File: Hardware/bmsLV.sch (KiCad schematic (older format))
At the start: 34 parts, among them J1 Conn_01x06_Male, J13 Conn_01x04_Male, J2 USB_B_Mini, J3 Conn_01x02_Female, J5 Conn_01x02_Female, K1 RM85V7, Q1 BSS138, SW1 SW_Push, U1 STM32F103C8Tx, Y1 Crystal

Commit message: Dash Led and jumpers
-output to Dash Led created
-added another jumper (J17) to ground
-J14, J15, J16 jumper position changed
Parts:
- added Q8: BSS138, Package_TO_SOT_SMD:SOT-23, symbol Transistor_FET:BSS138
- added R10: 100, Resistor_SMD:R_1206_3216Metric, symbol Device:R_Small
- added R17: 100K, Resistor_SMD:R_1206_3216Metric, symbol Device:R_Small
- added R41: 30, Resistor_SMD:R_1206_3216Metric, symbol Device:R_Small
- R39, R40: value 27 -> 30
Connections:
- net labels added: LED_D, LED_D_OUT
- wire segments 99 -> 106
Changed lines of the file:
@@
 EESchema Schematic File Version 4
-LIBS:bmsLV-cache
 EELAYER 30 0
 EELAYER END
@@
 $EndComp
 $Comp
-L Device:LED D4
-U 1 1 5FFAB034
-P 3750 5150
-F 0 "D4" H 3743 5366 50  0000 C CNN
-F 1 "LED" H 3743 5275 50  0000 C CNN
-F 2 "LED_SMD:LED_1206_3216Metric" H 3750 5150 50  0001 C CNN
-F 3 "~" H 3750 5150 50  0001 C CNN
-	1    3750 5150
-	-1   0    0    1
-$EndComp
-$Comp
 L Device:R_Small R4
 U 1 1 5FFAB03A
@@
 	-1   0    0    1
 $EndComp
-$Comp
-L power:GND #PWR?
-U 1 1 5FFFFAC8
-P 8300 2400
-AR Path="/5FAD7AC5/5FFFFAC8" Ref="#PWR?"  Part="1"
-AR Path="/5FFFFAC8" Ref="#PWR0101"  Part="1"
-F 0 "#PWR0101" H 8300 2150 50  0001 C CNN
-F 1 "GND" H 8305 2227 50  0000 C CNN
-F 2 "" H 8300 2400 50  0001 C CNN
-F 3 "" H 8300 2400 50  0001 C CNN
-	1    8300 2400
-	1    0    0    -1
-$EndComp
-Wire Wire Line
-	8300 2400 8150 2400
 Wire Wire Line
 	8150 2300 8300 2300
@@
 P 5800 5150
 F 0 "R39" V 5604 5150 50  0000 C CNN
-F 1 "27" V 5695 5150 50  0000 C CNN
+F 1 "30" V 5695 5150 50  0000 C CNN
 F 2 "Resistor_SMD:R_1206_3216Metric" H 5800 5150 50  0001 C CNN
 F 3 "~" H 5800 5150 50  0001 C CNN
@@
 P 5800 5250
 F 0 "R40" V 5604 5250 50  0000 C CNN
-F 1 "27" V 5695 5250 50  0000 C CNN
+F 1 "30" V 5695 5250 50  0000 C CNN
 F 2 "Resistor_SMD:R_1206_3216Metric" H 5800 5250 50  0001 C CNN
 F 3 "~" H 5800 5250 50  0001 C CNN
@@
 Wire Wire Line
 	5900 5250 6100 5250
+$Comp
+L Device:R_Small R17
+U 1 1 6076C183
+P 10250 4050
+F 0 "R17" H 10191 4004 50  0000 R CNN
+F 1 "100K" H 10191 4095 50  0000 R CNN
+F 2 "Resistor_SMD:R_1206_3216Metric" H 10250 4050 50  0001 C CNN
+F 3 "~" H 10250 4050 50  0001 C CNN
+	1    10250 4050
+	-1   0    0    1
+$EndComp
+Wire Wire Line
+	10250 4150 10250 4300
+$Comp
+L Device:R_Small R10
+U 1 1 60783A76
+P 10000 3800
+F 0 "R10" V 9804 3800 50  0000 C CNN
+F 1 "100" V 9895 3800 50  0000 C CNN
+F 2 "Resistor_SMD:R_1206_3216Metric" H 10000 3800 50  0001 C CNN
+F 3 "~" H 10000 3800 50  0001 C CNN
+	1    10000 3800
+	0    1    1    0
+$EndComp
+$Comp
+L Transistor_FET:BSS138 Q8
+U 1 1 60791F4D
+P 10650 3800
+F 0 "Q8" H 10855 3754 50  0000 L CNN
+F 1 "BSS138" H 10855 3845 50  0000 L CNN
+F 2 "Package_TO_SOT_SMD:SOT-23" H 10850 3725 50  0001 L CIN
+F 3 "https://www.fairchildsemi.com/datasheets/BS/BSS138.pdf" H 10650 3800 50  0001 L CNN
+	1    10650 3800
+	1    0    0    -1
+$EndComp
+$Comp
+L power:GND #PWR0108
+U 1 1 607B5692
+P 10750 4050
+F 0 "#PWR0108" H 10750 3800 50  0001 C CNN
+F 1 "GND" H 10755 3877 50  0000 C CNN
+F 2 "" H 10750 4050 50  0001 C CNN
+F 3 "" H 10750 4050 50  0001 C CNN
+	1    10750 4050
+	1    0    0    -1
+$EndComp
+$Comp
+L power:GND #PWR0101
+U 1 1 607DED82
+P 10250 4300
+F 0 "#PWR0101" H 10250 4050 50  0001 C CNN
+F 1 "GND" H 10255 4127 50  0000 C CNN
+F 2 "" H 10250 4300 50  0001 C CNN
+F 3 "" H 10250 4300 50  0001 C CNN
+	1    10250 4300
+	1    0    0    -1
+$EndComp
+Wire Wire Line
+	10750 4050 10750 4000
+Wire Wire Line
+	10450 3800 10250 3800
+Wire Wire Line
+	10250 3800 10250 3950
+Wire Wire Line
+	10250 3800 10100 3800
+Connection ~ 10250 3800
+Wire Wire Line
+	9900 3800 9800 3800
+$Comp
+L Device:LED D4
+U 1 1 5FFAB034
+P 3750 5150
+F 0 "D4" H 3743 5366 50  0000 C CNN
+F 1 "LED" H 3743 5275 50  0000 C CNN
+F 2 "LED_SMD:LED_1206_3216Metric" H 3750 5150 50  0001 C CNN
+F 3 "~" H 3750 5150 50  0001 C CNN
+	1    3750 5150
+	-1   0    0    1
+$EndComp
+Text GLabel 4200 5250 0    50   Input ~ 0
+LED_D
+Text GLabel 9800 3800 0    50   Input ~ 0
+LED_D
+Wire Wire Line
+	10750 3600 10750 3400
+Text GLabel 10750 3100 0    50   Input ~ 0
+LED_D_OUT
+Text GLabel 8150 2400 2    50   Input ~ 0
+LED_D_OUT
+$Comp
+L Device:R_Small R41
+U 1 1 60860F48
+P 10750 3300
+F 0 "R41" H 10809 3346 50  0000 L CNN
+F 1 "30" H 10809 3255 50  0000 L CNN
+F 2 "Resistor_SMD:R_1206_3216Metric" H 10750 3300 50  0001 C CNN
+F 3 "~" H 10750 3300 50  0001 C CNN
+	1    10750 3300
+	1    0    0    -1
+$EndComp
+Wire Wire Line
+	10750 3100 10750 3200
 $EndSCHEMATC

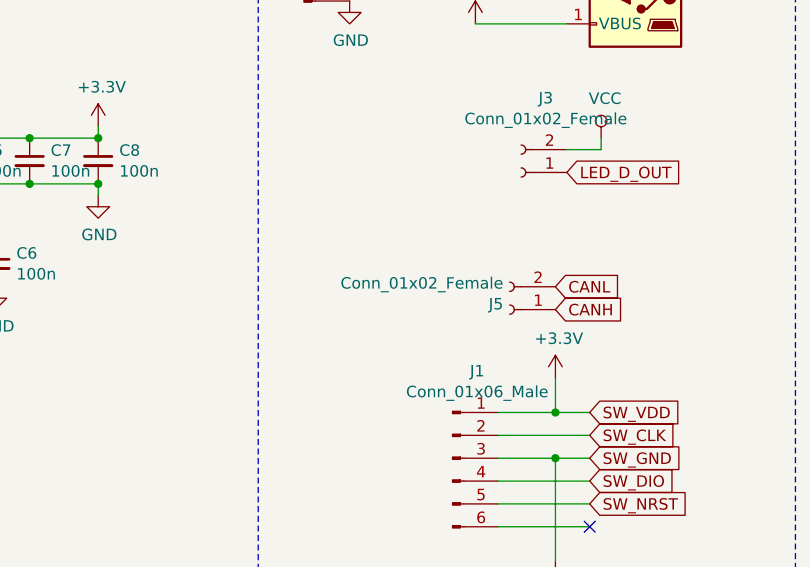
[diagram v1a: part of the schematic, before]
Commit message: Connector footrpint changed
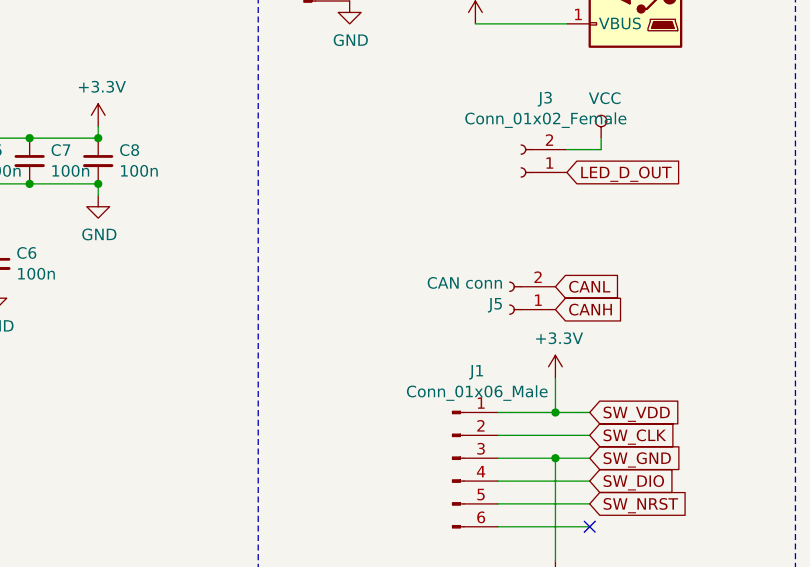
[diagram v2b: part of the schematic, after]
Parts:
- J3: footprint TerminalBlock:TerminalBlock_bornier-2_P5.08mm -> Connector_Phoenix_MSTB:PhoenixContact_MSTBVA_2,5_2-G-5,08_1x02_P5.08mm_Vertical
- J5: value Conn_01x02_Female -> CAN conn; footprint TerminalBlock:TerminalBlock_bornier-2_P5.08mm -> Connector_Phoenix_MSTB:PhoenixContact_MSTBVA_2,5_2-G-5,08_1x02_P5.08mm_Vertical
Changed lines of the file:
@@
 F 0 "J3" H 7842 2075 50  0000 C CNN
 F 1 "Conn_01x02_Female" H 7842 2166 50  0000 C CNN
-F 2 "TerminalBlock:TerminalBlock_bornier-2_P5.08mm" H 7950 2400 50  0001 C CNN
+F 2 "Connector_Phoenix_MSTB:PhoenixContact_MSTBVA_2,5_2-G-5,08_1x02_P5.08mm_Vertical" H 7950 2400 50  0001 C CNN
 F 3 "~" H 7950 2400 50  0001 C CNN
 	1    7950 2400
@@
 AR Path="/60009E9A" Ref="J5"  Part="1"
 F 0 "J5" H 7928 2976 50  0000 L CNN
-F 1 "Conn_01x02_Female" H 7928 2885 50  0000 L CNN
-F 2 "TerminalBlock:TerminalBlock_bornier-2_P5.08mm" H 7900 3000 50  0001 C CNN
+F 1 "CAN conn" H 7928 2885 50  0000 L CNN
+F 2 "Connector_Phoenix_MSTB:PhoenixContact_MSTBVA_2,5_2-G-5,08_1x02_P5.08mm_Vertical" H 7900 3000 50  0001 C CNN
 F 3 "~" H 7900 3000 50  0001 C CNN
 	1    7900 3000

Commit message: STM changed
Due to the lack of processors on market, we decided to change STM32F103C8T6 for STM32F4P5RET. So the schematic and PCB is significantly changed in this area.
Furthermore, the library and footprint to new processor was added.
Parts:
- removed U1: STM32F103C8Tx, Package_QFP:LQFP-48_7x7mm_P0.5mm, symbol MCU_ST_STM32F1:STM32F103C8Tx
- added C36: 100n, Capacitor_SMD:C_1206_3216Metric, symbol Device:C_Small
- added R52, R59: 2.2k, Resistor_SMD:R_1206_3216Metric, symbol Device:R_Small
- added U5: STM32L4P5RET6, footprints:STM32L4P5RET6, symbol 2021-04-28_23-52-00:STM32L4P5RET6
- K1: footprint RM85V7:RM85V7 -> footprints:RM85V7
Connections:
- net labels added: VBAT
- wire segments 106 -> 126
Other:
- moved on the sheet: C1, C2, C3, C4, C5, C6, C7, C8, D1, D16, D2, D3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

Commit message: CS and CLK pull up added
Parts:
- added R60, R61: 2.2k, Resistor_SMD:R_1206_3216Metric, symbol Device:R_Small
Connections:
- wire segments 126 -> 118
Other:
- moved on the sheet: R52, R59
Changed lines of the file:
@@
 Text GLabel 3350 2650 0    50   Input ~ 0
 CS
-Text GLabel 2400 3550 0    50   Input ~ 0
-MOSI
-Text GLabel 2400 3200 0    50   Input ~ 0
-MISO
-Text GLabel 3350 3150 0    50   Input ~ 0
-SCK
 Wire Wire Line
 	2750 3950 2650 3950
@@
 	0    -1   -1   0
 $EndComp
-Wire Wire Line
-	3350 3350 3200 3350
 $Comp
 L power:+3.3V #PWR0109
 U 1 1 608FC828
-P 2850 3350
-F 0 "#PWR0109" H 2850 3200 50  0001 C CNN
-F 1 "+3.3V" H 2865 3523 50  0000 C CNN
-F 2 "" H 2850 3350 50  0001 C CNN
-F 3 "" H 2850 3350 50  0001 C CNN
-	1    2850 3350
+P 3200 4850
+F 0 "#PWR0109" H 3200 4700 50  0001 C CNN
+F 1 "+3.3V" H 3215 5023 50  0000 C CNN
+F 2 "" H 3200 4850 50  0001 C CNN
+F 3 "" H 3200 4850 50  0001 C CNN
+	1    3200 4850
 	1    0    0    -1
 $EndComp
@@
 L Device:R_Small R52
 U 1 1 60947006
-P 2650 3100
-F 0 "R52" V 2454 3100 50  0000 C CNN
-F 1 "2.2k" V 2545 3100 50  0000 C CNN
-F 2 "Resistor_SMD:R_1206_3216Metric" H 2650 3100 50  0001 C CNN
-F 3 "~" H 2650 3100 50  0001 C CNN
-	1    2650 3100
-	1    0    0    -1
-$EndComp
-Wire Wire Line
-	3200 3350 3200 3550
+P 2900 4950
+F 0 "R52" V 2704 4950 50  0000 C CNN
+F 1 "2.2k" V 2795 4950 50  0000 C CNN
+F 2 "Resistor_SMD:R_1206_3216Metric" H 2900 4950 50  0001 C CNN
+F 3 "~" H 2900 4950 50  0001 C CNN
+	1    2900 4950
+	1    0    0    -1
+$EndComp
 Wire Wire Line
 	7900 3650 8150 3650
@@
 L power:+3.3V #PWR0110
 U 1 1 608E3DB7
-P 2650 3000
-F 0 "#PWR0110" H 2650 2850 50  0001 C CNN
-F 1 "+3.3V" H 2665 3173 50  0000 C CNN
-F 2 "" H 2650 3000 50  0001 C CNN
-F 3 "" H 2650 3000 50  0001 C CNN
-	1    2650 3000
+P 2900 4850
+F 0 "#PWR0110" H 2900 4700 50  0001 C CNN
+F 1 "+3.3V" H 2915 5023 50  0000 C CNN
+F 2 "" H 2900 4850 50  0001 C CNN
+F 3 "" H 2900 4850 50  0001 C CNN
+	1    2900 4850
 	1    0    0    -1
 $EndComp
@@
 Wire Wire Line
 	2950 2750 3300 2750
-Wire Wire Line
-	2400 3200 2650 3200
-Wire Wire Line
-	2850 3550 3200 3550
-Connection ~ 2850 3550
 $Comp
 L Device:R_Small R59
 U 1 1 609402DB
-P 2850 3450
-F 0 "R59" V 2654 3450 50  0000 C CNN
-F 1 "2.2k" V 2745 3450 50  0000 C CNN
-F 2 "Resistor_SMD:R_1206_3216Metric" H 2850 3450 50  0001 C CNN
-F 3 "~" H 2850 3450 50  0001 C CNN
-	1    2850 3450
-	1    0    0    -1
-$EndComp
-Wire Wire Line
-	3350 3250 3100 3250
-Wire Wire Line
-	3100 3250 3100 3200
-Wire Wire Line
-	3100 3200 2650 3200
-Connection ~ 2650 3200
+P 3200 4950
+F 0 "R59" V 3004 4950 50  0000 C CNN
+F 1 "2.2k" V 3095 4950 50  0000 C CNN
+F 2 "Resistor_SMD:R_1206_3216Metric" H 3200 4950 50  0001 C CNN
+F 3 "~" H 3200 4950 50  0001 C CNN
+	1    3200 4950
+	1    0    0    -1
+$EndComp
 Wire Wire Line
 	3250 2850 3250 3050
 Wire Wire Line
 	3300 2750 3300 2950
-Wire Wire Line
-	2400 3550 2850 3550
+$Comp
+L Device:R_Small R61
+U 1 1 6093F57C
+P 2650 4950
+F 0 "R61" V 2454 4950 50  0000 C CNN
+F 1 "2.2k" V 2545 4950 50  0000 C CNN
+F 2 "Resistor_SMD:R_1206_3216Metric" H 2650 4950 50  0001 C CNN
+F 3 "~" H 2650 4950 50  0001 C CNN
+	1    2650 4950
+	1    0    0    -1
+$EndComp
+$Comp
+L power:+3.3V #PWR0111
+U 1 1 6093F582
+P 2650 4850
+F 0 "#PWR0111" H 2650 4700 50  0001 C CNN
+F 1 "+3.3V" H 2665 5023 50  0000 C CNN
+F 2 "" H 2650 4850 50  0001 C CNN
+F 3 "" H 2650 4850 50  0001 C CNN
+	1    2650 4850
+	1    0    0    -1
+$EndComp
+$Comp
+L Device:R_Small R60
+U 1 1 60944A92
+P 2400 4950
+F 0 "R60" V 2204 4950 50  0000 C CNN
+F 1 "2.2k" V 2295 4950 50  0000 C CNN
+F 2 "Resistor_SMD:R_1206_3216Metric" H 2400 4950 50  0001 C CNN
+F 3 "~" H 2400 4950 50  0001 C CNN
+	1    2400 4950
+	1    0    0    -1
+$EndComp
+$Comp
+L power:+3.3V #PWR0112
+U 1 1 60944A98
+P 2400 4850
+F 0 "#PWR0112" H 2400 4700 50  0001 C CNN
+F 1 "+3.3V" H 2415 5023 50  0000 C CNN
+F 2 "" H 2400 4850 50  0001 C CNN
+F 3 "" H 2400 4850 50  0001 C CNN
+	1    2400 4850
+	1    0    0    -1
+$EndComp
+Text GLabel 2400 5050 3    50   Input ~ 0
+SCK
+Text GLabel 2900 5050 3    50   Input ~ 0
+MISO
+Text GLabel 3200 5050 3    50   Input ~ 0
+MOSI
+Text GLabel 3350 3150 0    50   Input ~ 0
+SCK
+Text GLabel 3350 3250 0    50   Input ~ 0
+MISO
+Text GLabel 3350 3350 0    50   Input ~ 0
+MOSI
+Text GLabel 2650 5050 3    50   Input ~ 0
+CS
 $EndSCHEMATC

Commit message: Some changes
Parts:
- K1: symbol RM85V7:RM85V7 -> bmsLV-rescue:RM85V7-RM85V7
- U5: symbol 2021-04-28_23-52-00:STM32L4P5RET6 -> bmsLV-rescue:STM32L4P5RET6-2021-04-28_23-52-00
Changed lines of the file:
@@
 EESchema Schematic File Version 4
-EELAYER 30 0
+LIBS:bmsLV-cache
+EELAYER 29 0
 EELAYER END
 $Descr A4 11693 8268
@@
 	3950 5500 3900 5500
 $Comp
-L 2021-04-28_23-52-00:STM32L4P5RET6 U5
+L bmsLV-rescue:STM32L4P5RET6-2021-04-28_23-52-00 U5
 U 2 1 60A02C99
 P 3950 5000
@@
 Term_5
 $Comp
-L 2021-04-28_23-52-00:STM32L4P5RET6 U5
+L bmsLV-rescue:STM32L4P5RET6-2021-04-28_23-52-00 U5
 U 1 1 608DF93C
 P 3350 1150
@@
 Connection ~ 2750 6450
 $Comp
-L RM85V7:RM85V7 K1
+L bmsLV-rescue:RM85V7-RM85V7 K1
 U 1 1 608C3AB8
 P 3100 6500
@@
 U 1 1 60947006
 P 2900 4950
-F 0 "R52" V 2704 4950 50  0000 C CNN
-F 1 "2.2k" V 2795 4950 50  0000 C CNN
+F 0 "R52" V 2750 4950 50  0000 C CNN
+F 1 "2.2k" V 2850 4950 50  0000 C CNN
 F 2 "Resistor_SMD:R_1206_3216Metric" H 2900 4950 50  0001 C CNN
 F 3 "~" H 2900 4950 50  0001 C CNN

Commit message: Software update 3
Current sensor added to PCB (through wires)
Current sensor handling added
Cell balance working! (HUGE PART OF UPDATE)
CheckError function modified (a lot of more error added)
Serial print function added (not tested)
+ some cosmetic changes
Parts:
- C1, C2, C3, C36, C4, C5, C6, C7, C8: symbol Device:C_Small -> bmsLV-rescue:C_Small-Device
- D1, D2, D3, D4: symbol Device:LED -> bmsLV-rescue:LED-Device
- D16: symbol Device:D_Small -> bmsLV-rescue:D_Small-Device
- J1: symbol Connector:Conn_01x06_Male -> bmsLV-rescue:Conn_01x06_Male-Connector
- J13: symbol Connector:Conn_01x04_Male -> bmsLV-rescue:Conn_01x04_Male-Connector
- J2: symbol Connector:USB_B_Mini -> bmsLV-rescue:USB_B_Mini-Connector
- J3, J5: symbol Connector:Conn_01x02_Female -> bmsLV-rescue:Conn_01x02_Female-Connector
- L1: symbol Device:L_Small -> bmsLV-rescue:L_Small-Device
- Q1, Q8: symbol Transistor_FET:BSS138 -> bmsLV-rescue:BSS138-Transistor_FET
- R1, R10, R17, R2, R3, R39, R4, R40, R41, R5, R52, R59, R6, R60, R61, R7, R8: symbol Device:R_Small -> bmsLV-rescue:R_Small-Device
- SW1: symbol Switch:SW_Push -> bmsLV-rescue:SW_Push-Switch
- Y1: symbol Device:Crystal -> bmsLV-rescue:Crystal-Device
